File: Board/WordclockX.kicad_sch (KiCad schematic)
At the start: 138 parts, among them J1 USB_C_Receptacle_USB2.0, SW1 SW_Push_Dual, SW2 SW_Push_Dual, U1 W25Q16JLSNIG, U2 MCP7940N-xST, U3 RP2040, U4 MIC5504-3.3YM5, U5 74HCT137, U6 PCA9626, U7 PCA9626, U8 171010550, Y1 12M, Y2 32768

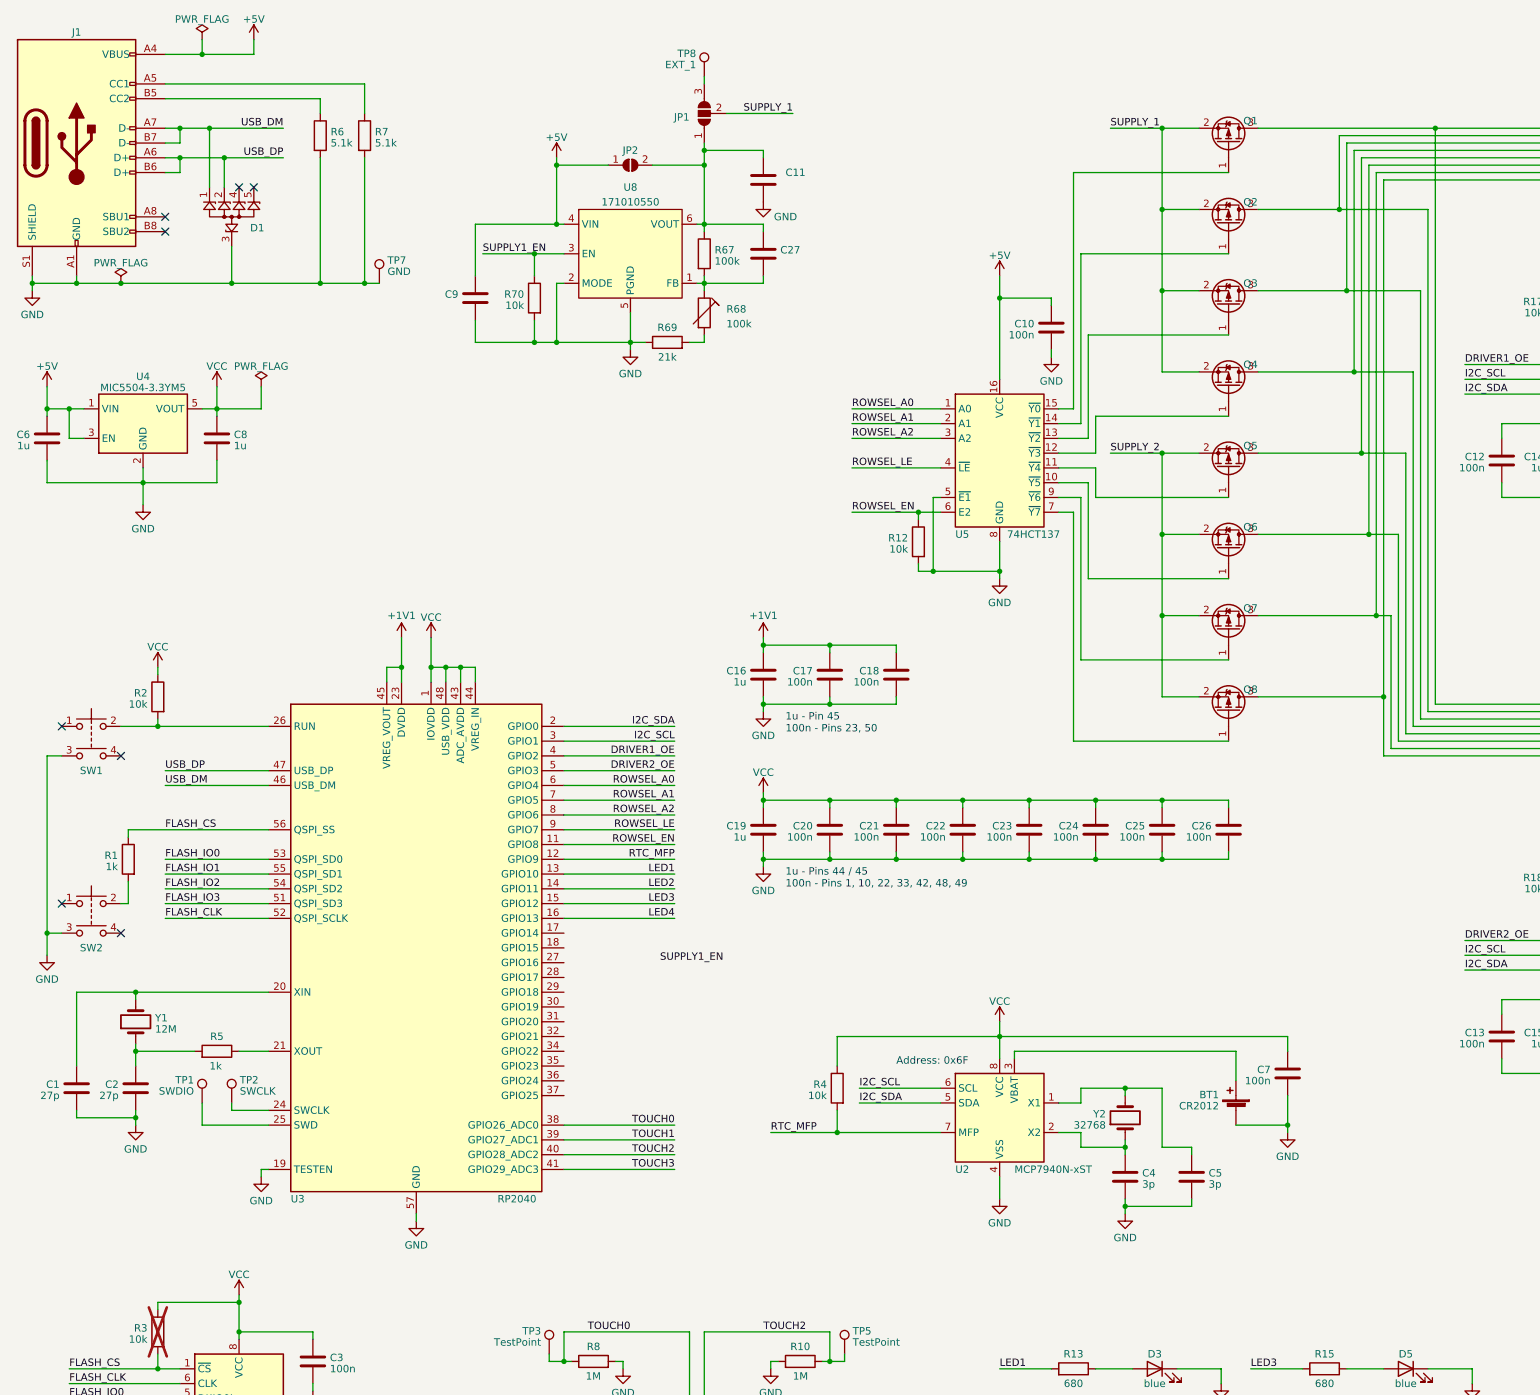
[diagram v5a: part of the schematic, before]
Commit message: Finished adding voltage regulators
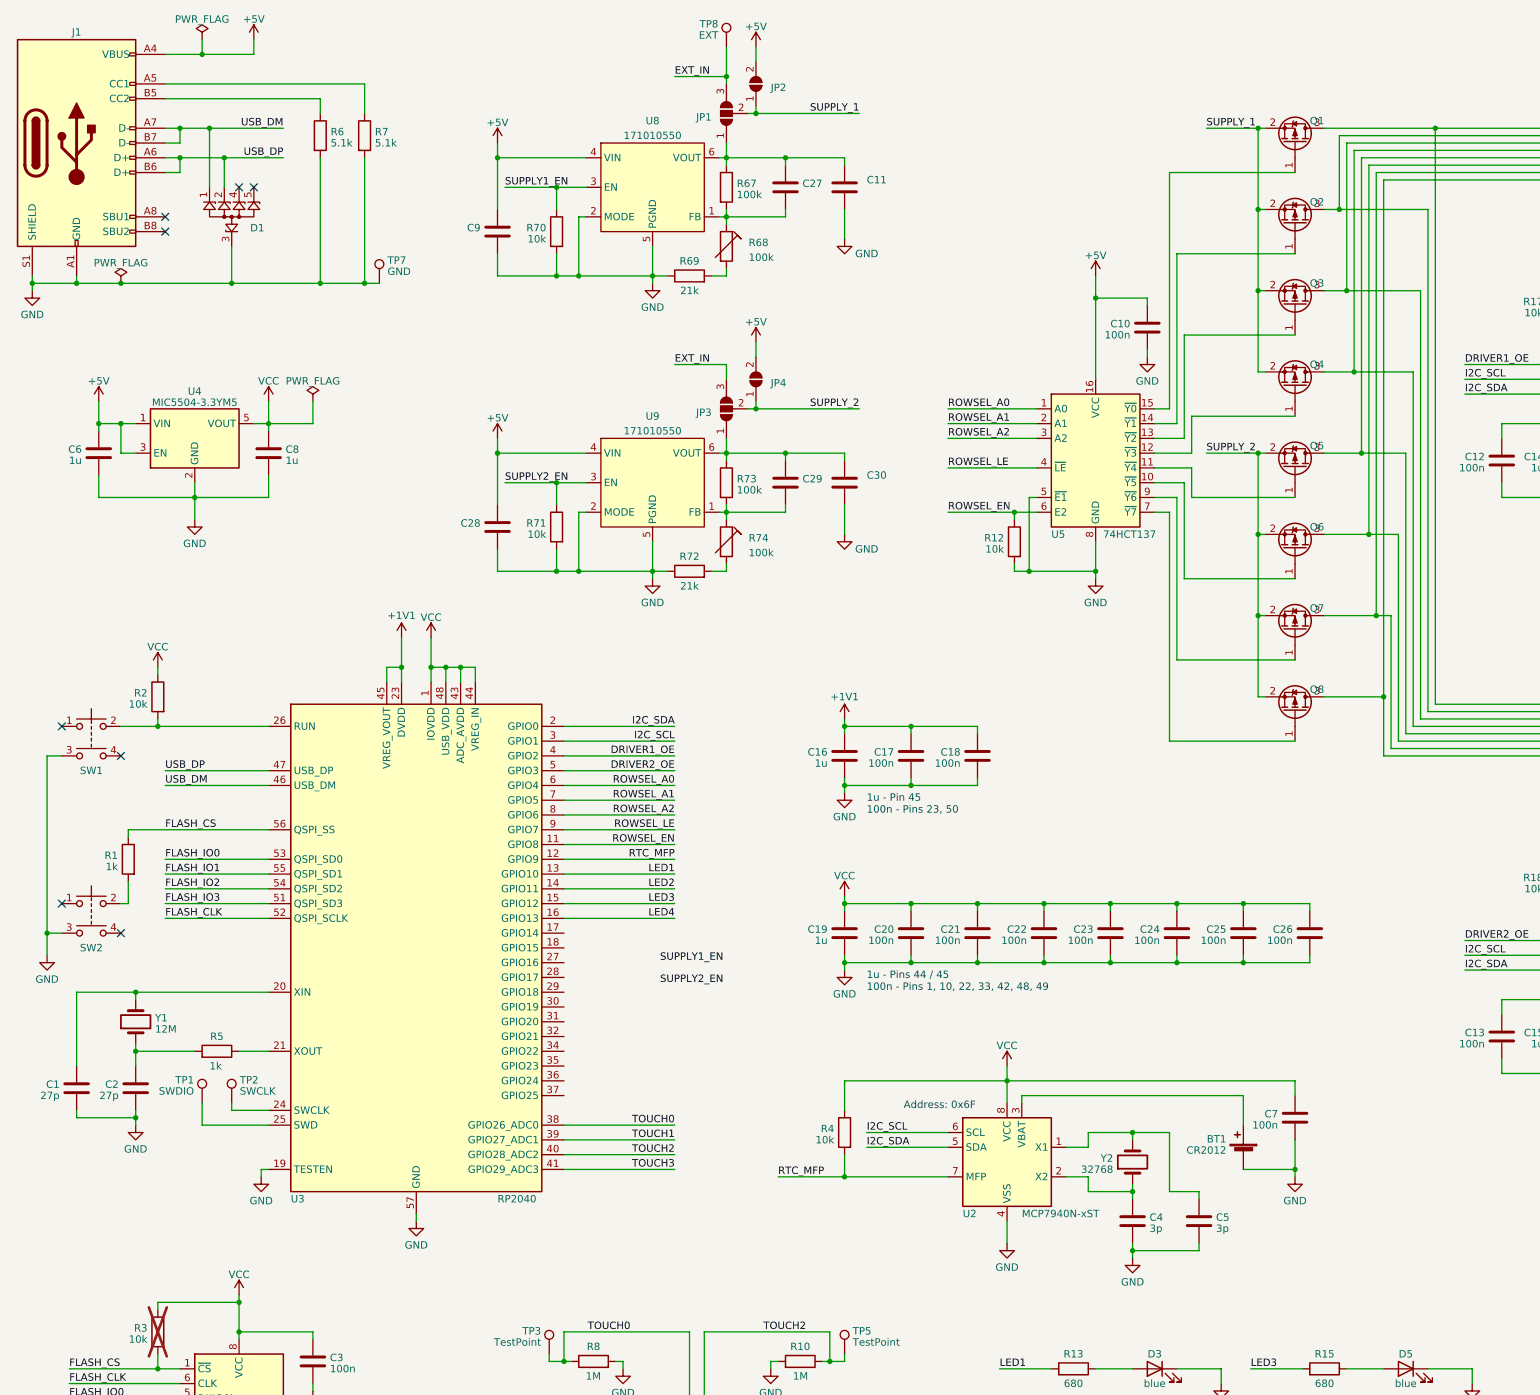
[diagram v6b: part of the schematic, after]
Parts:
- added C28, C29, C30: ~, symbol Device:C
- added JP3: SolderJumper_3_Open, symbol Jumper:SolderJumper_3_Open
- added JP4: SolderJumper_2_Open, symbol Jumper:SolderJumper_2_Open
- added R71: 10k, Resistor_SMD:R_0603_1608Metric, symbol Device:R
- added R72: 21k, Resistor_SMD:R_0603_1608Metric, symbol Device:R
- added R73: 100k, Resistor_SMD:R_0603_1608Metric, symbol Device:R
- added R74: 100k, symbol Device:R_Trim
- added U9: 171010550, Wordclock:LGA-6EP_2.5x2.5, symbol Wordclock:171010550
- TP8: value EXT_1 -> EXT
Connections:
- net +5V: now also JP2.2 (B), C28.1, JP4.2 (B), U9.4 (VIN); no longer JP2.1 (A)
- net GND: now also C28.2, C30.2, R71.2, R72.1, U9.2 (MODE), U9.5 (PGND), U9.EP (PGND)
- net SUPPLY_1: now also JP2.1 (A)
- net SUPPLY_2: now also JP3.2 (C), JP4.1 (A)
- net at C11.1, C27.1, JP1.1 (A)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: no longer JP2.2 (B)
- net EXT_IN: now reaches JP1.3 (B), TP8.1
- net EXT_IN: now also JP3.3 (B)
- new net: C29.1, C30.1, JP3.1 (A), R73.1, U9.6 (VOUT)
- new net: R72.2, R74.2
- new net: C29.2, R73.2, R74.1, U9.1 (FB)
- new net SUPPLY2_EN: R71.1, U9.3 (EN)
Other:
- moved on the sheet: BT1, C10, C11, C16, C17, C18, C19, C20, C21, C22, C23, C24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

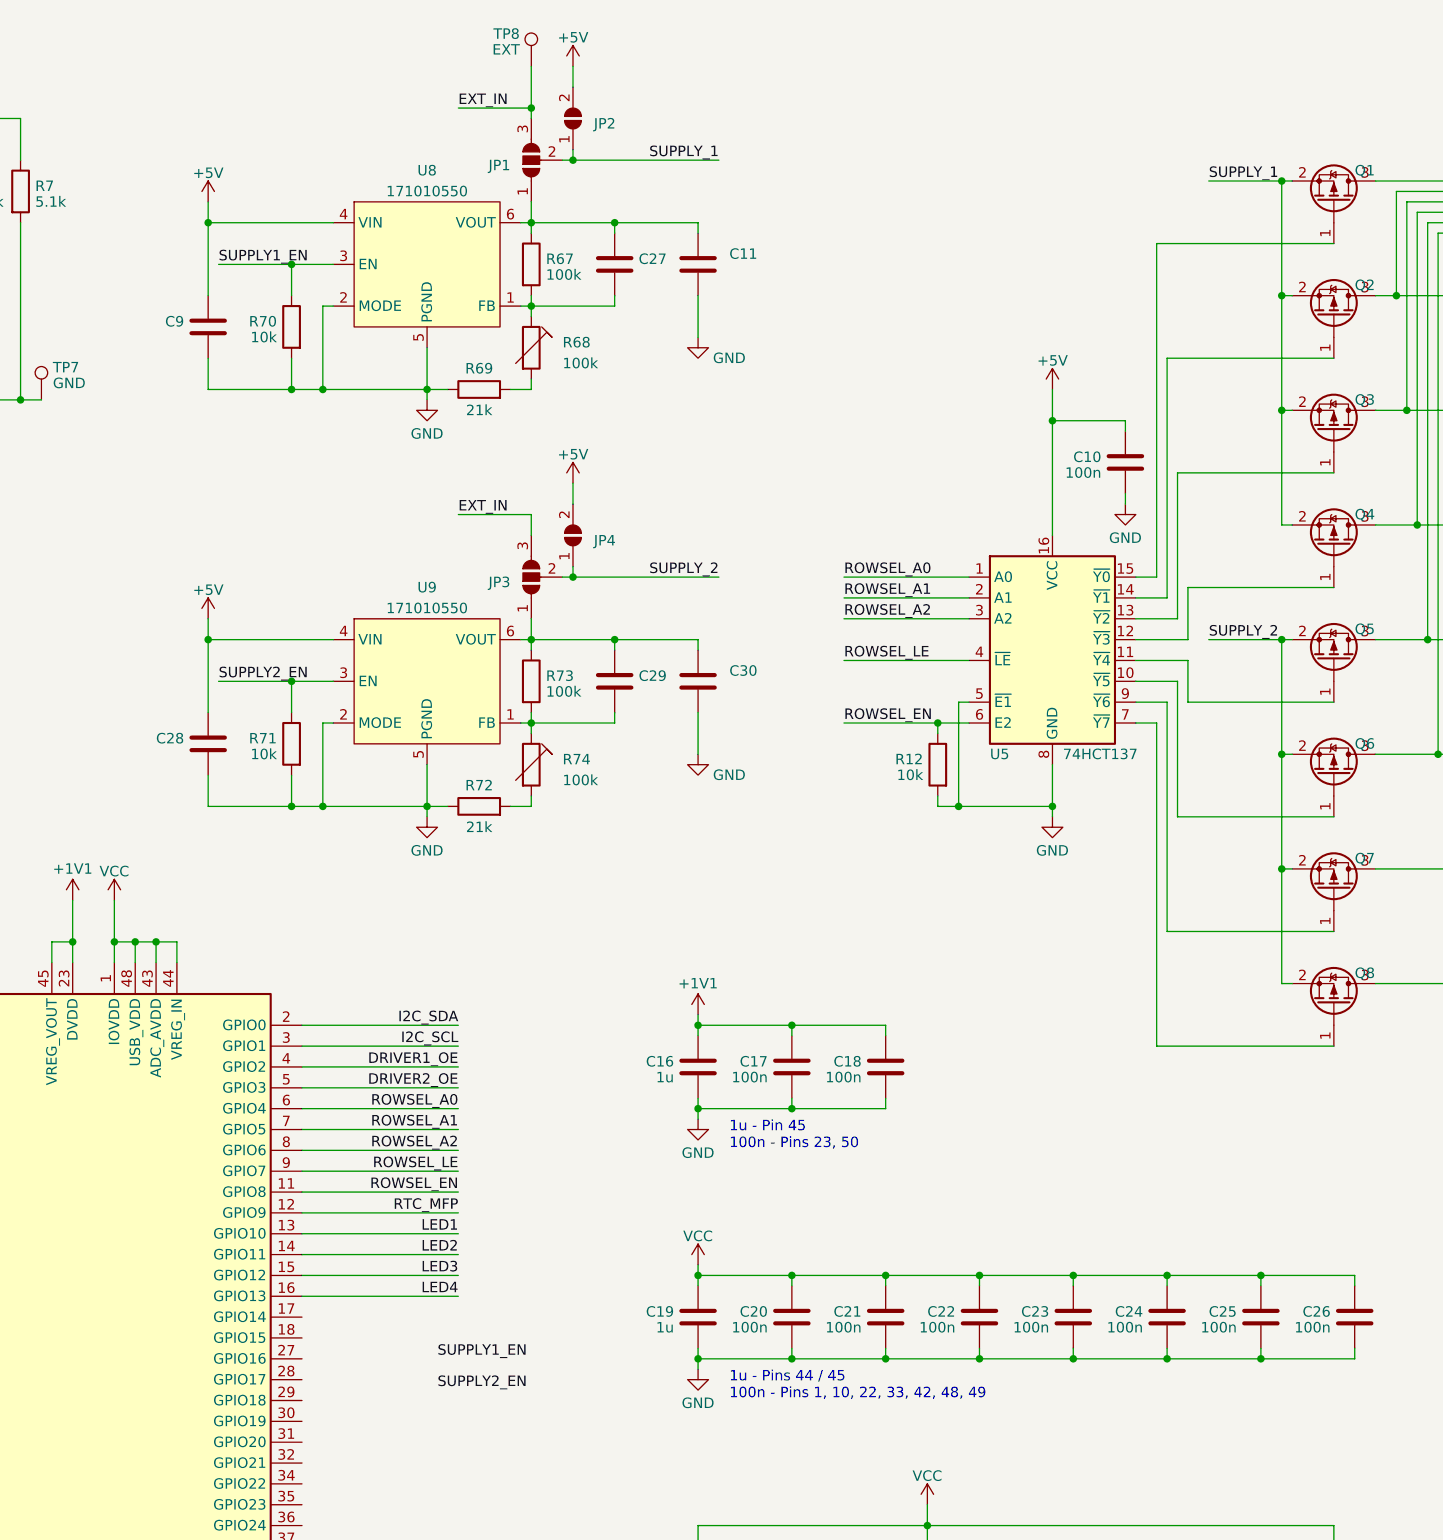
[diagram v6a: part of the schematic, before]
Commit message: Removed regulators again, probably overkill
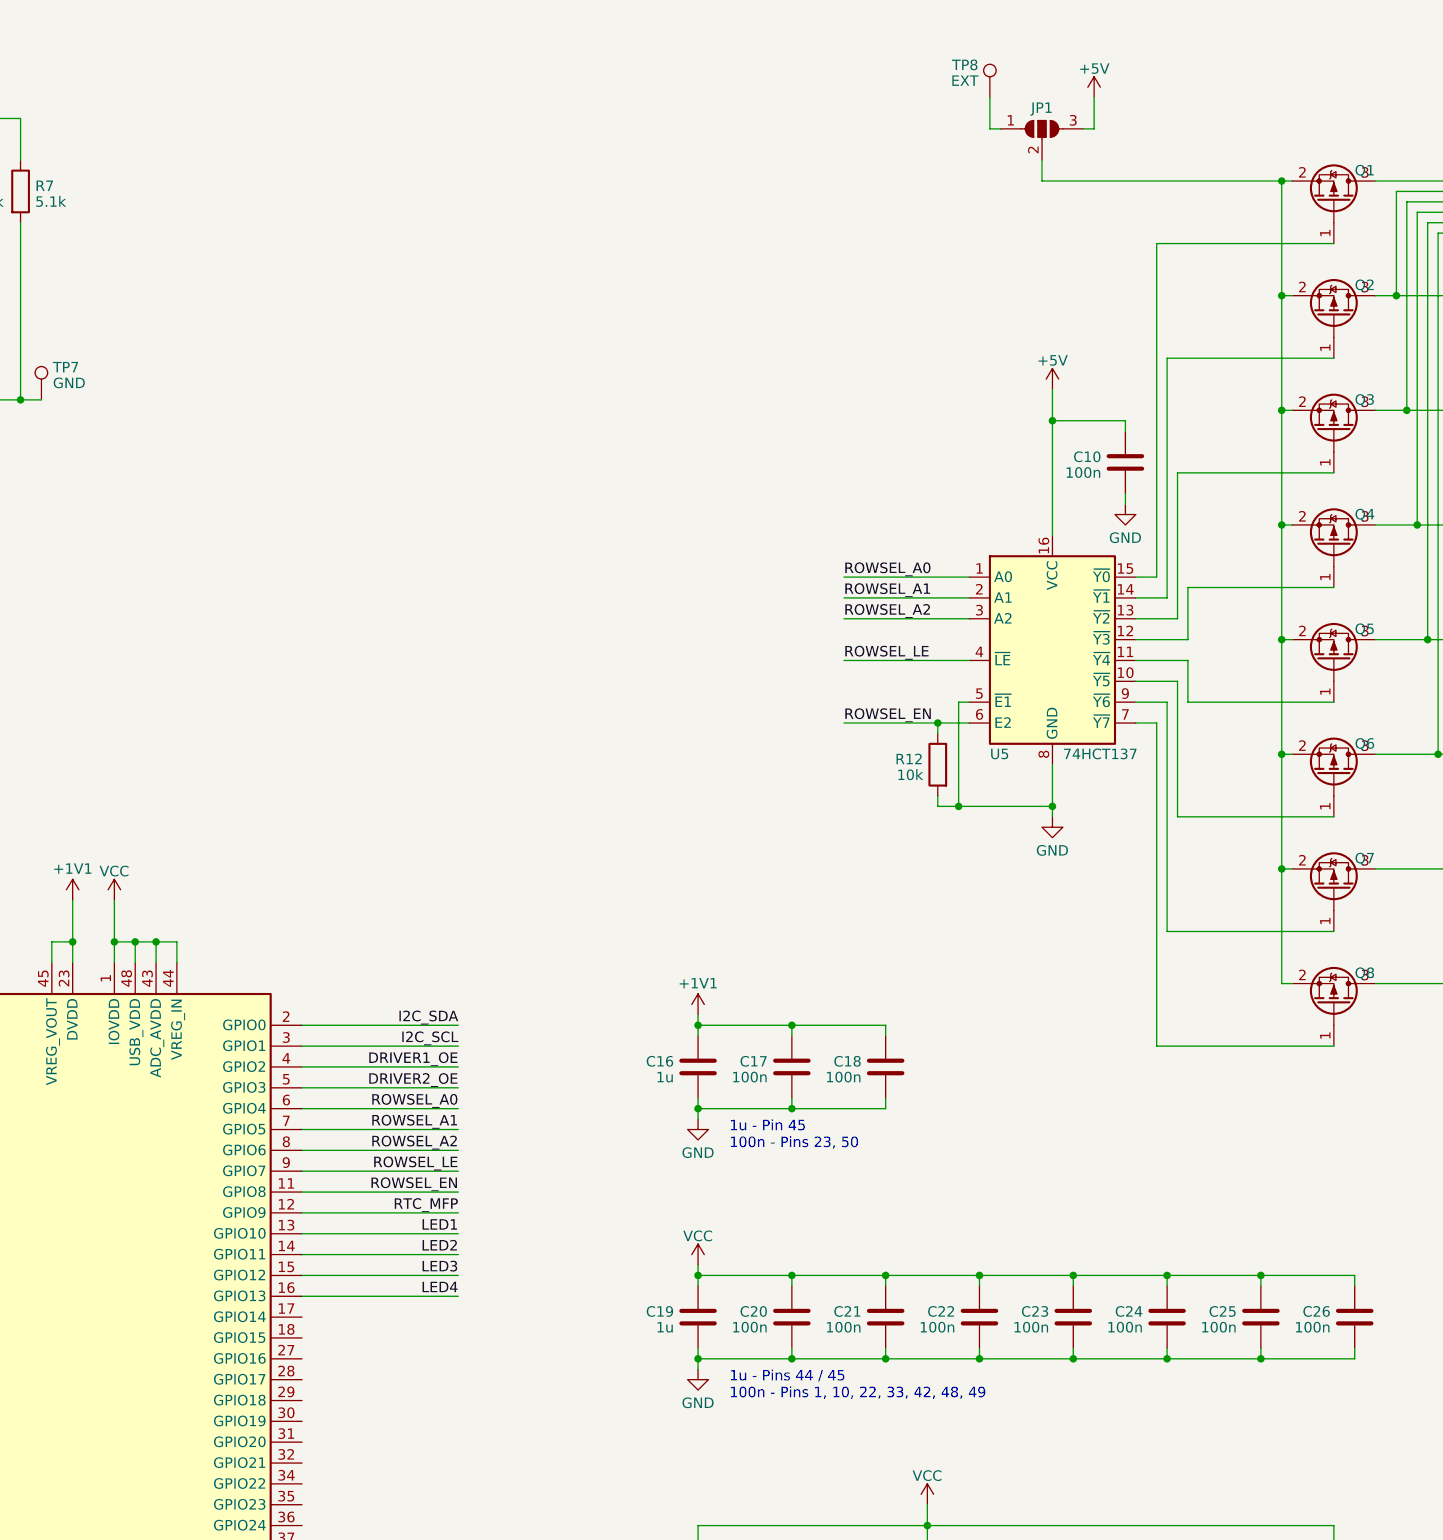
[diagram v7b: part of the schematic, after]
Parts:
- removed C11, C27, C28, C29, C30, C9: ~, symbol Device:C
- removed JP2, JP4: SolderJumper_2_Open, symbol Jumper:SolderJumper_2_Open
- removed JP3: SolderJumper_3_Open, symbol Jumper:SolderJumper_3_Open
- removed R67, R73: 100k, Resistor_SMD:R_0603_1608Metric, symbol Device:R
- removed R68, R74: 100k, symbol Device:R_Trim
- removed R69, R72: 21k, Resistor_SMD:R_0603_1608Metric, symbol Device:R
- removed R70, R71: 10k, Resistor_SMD:R_0603_1608Metric, symbol Device:R
- removed U8, U9: 171010550, Wordclock:LGA-6EP_2.5x2.5, symbol Wordclock:171010550
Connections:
- net SUPPLY_2 is gone; now on an unnamed net: Q5.2 (S), Q6.2 (S), Q7.2 (S), Q8.2 (S)
- net +5V: now also JP1.3 (B)
- net at JP1.1 (A): now also TP8.1
- removed net EXT_IN: JP1.3 (B), TP8.1
- net SUPPLY_1: no longer names the net of JP1.2 (C), Q1.2 (S), Q2.2 (S), Q3.2 (S), Q4.2 (S)
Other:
- moved on the sheet: TP8
